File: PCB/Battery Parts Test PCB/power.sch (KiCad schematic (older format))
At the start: 28 parts, among them P4 CONN_2, P5 PWR_SWITCH, P6 CONN_2, Q10 FET_N, Q11 FET_N, Q9 FET_N, U1 ISL94203

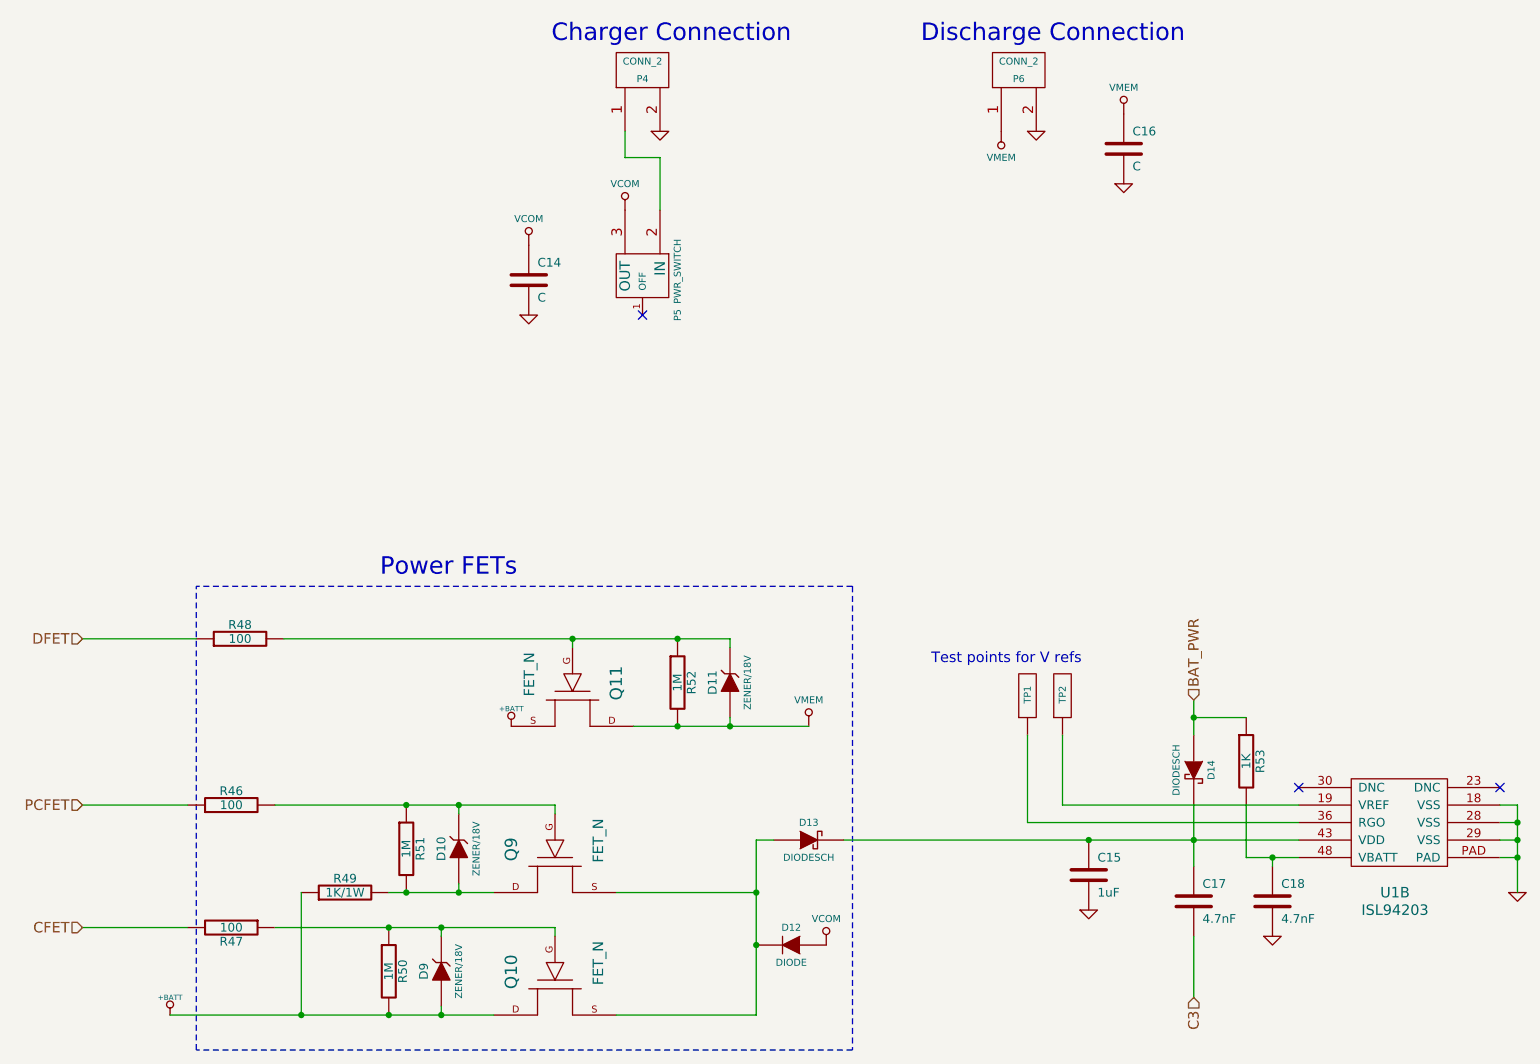
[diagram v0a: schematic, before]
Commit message: finished schematic with new battery monitor
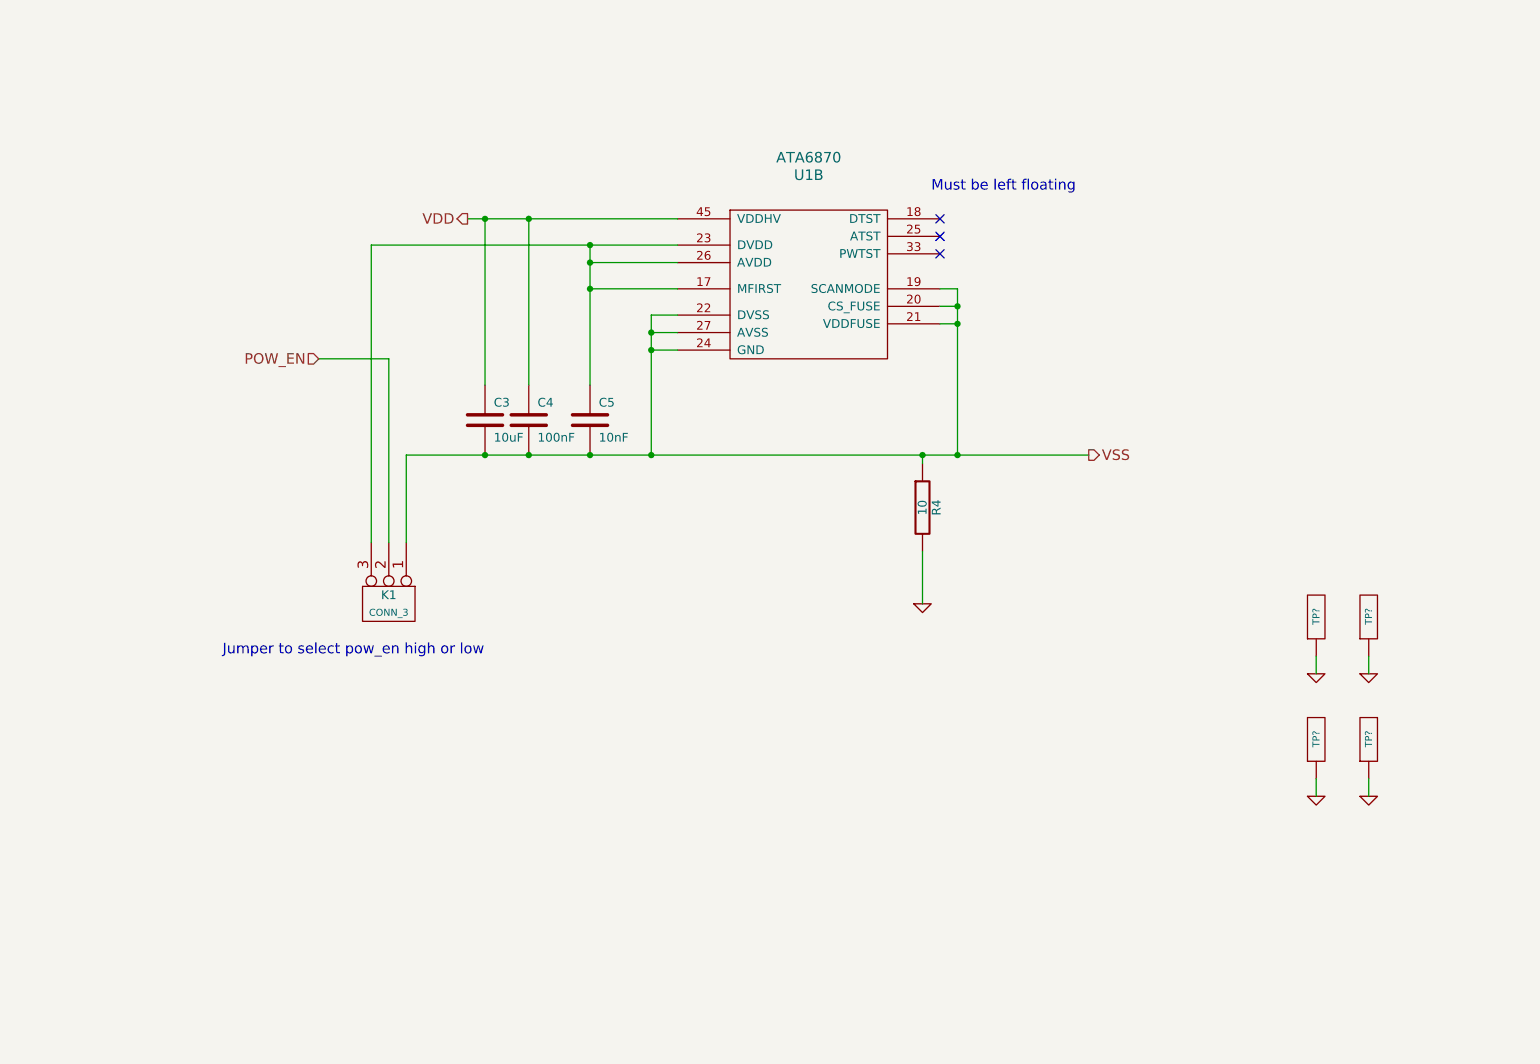
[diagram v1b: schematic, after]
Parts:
- removed C14, C16: C, symbol C
- removed C15: 1uF, symbol C
- removed C17, C18: 4.7nF, symbol C
- removed D10, D11, D9: ZENER/18V, symbol ZENER
- removed D12: DIODE, symbol DIODE
- removed D13, D14: DIODESCH, symbol DIODESCH
- removed P4, P6: CONN_2, symbol CONN_2
- removed P5: PWR_SWITCH, symbol PWR_SWITCH
- removed Q10, Q11, Q9: FET_N, symbol FET_N
- removed R46, R47, R48: 100, symbol R
- removed R49: 1K/1W, symbol R
- removed R50, R51, R52: 1M, symbol R
- removed R53: 1K, symbol R
- removed TP1, TP2: TEST_POINT, symbol TEST_POINT
- removed U1: ISL94203, symbol ISL94203
- added C3: 10uF, symbol C
- added C4: 100nF, symbol C
- added C5: 10nF, symbol C
- added K1: CONN_3, symbol CONN_3
- added R4: 10, symbol R
- added TP? (x4): TEST_POINT, symbol TEST_POINT
- added U1: ATA6870, symbol ATA6870
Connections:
- net GND: now also R4.2, TP?.1, TP?.1, TP?.1, TP?.1
- new net: C5.1, K1.3 (P3), U1.17 (MFIRST), U1.23 (DVDD), U1.26 (AVDD)
- new net POW_EN: K1.2 (PM)
- new net VDD: C3.1, C4.1, U1.45 (VDDHV)
- new net VSS: C3.2, C4.2, C5.2, K1.1 (P1), R4.1, U1.19 (SCANMODE), U1.20 (CS_FUSE), U1.21 (VDDFUSE), U1.22 (DVSS), U1.24 (GND), U1.27 (AVSS)
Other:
- note added: "Jumper to select pow_en high or low"
- note added: "Must be left floating"
- note removed: "Charger Connection"
- note removed: "Discharge Connection"
- note removed: "Power FETs"
- note removed: "Test points for V refs"

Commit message: updated schematic
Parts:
- gave numbers to parts that had none: 4
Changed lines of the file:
@@
-EESchema Schematic File Version 2  date 4/30/2013 1:48:29 PM
+EESchema Schematic File Version 2  date 5/7/2013 3:13:49 PM
 LIBS:power
 LIBS:device
@@
 Sheet 3 9
 Title ""
-Date "30 apr 2013"
+Date "7 may 2013"
 Rev ""
 Comp ""
@@
 $EndDescr
 $Comp
-L TEST_POINT TP?
+L TEST_POINT TP5
 U 1 1 5178A9A6
 P 8800 5200
-F 0 "TP?" H 8830 5200 40  0000 L CNN
+F 0 "TP5" H 8830 5200 40  0000 L CNN
 F 1 "TEST_POINT" H 8900 5105 30  0001 C CNN
 	1    8800 5200
@@
 $EndComp
 $Comp
-L GND #PWR?
+L GND #PWR01
 U 1 1 5178A9A5
 P 8800 5450
-F 0 "#PWR?" H 8800 5450 30  0001 C CNN
+F 0 "#PWR01" H 8800 5450 30  0001 C CNN
 F 1 "GND" H 8800 5380 30  0001 C CNN
 	1    8800 5450
@@
 	9100 5350 9100 5450
 $Comp
-L GND #PWR?
+L GND #PWR02
 U 1 1 5178A9A4
 P 9100 5450
-F 0 "#PWR?" H 9100 5450 30  0001 C CNN
+F 0 "#PWR02" H 9100 5450 30  0001 C CNN
 F 1 "GND" H 9100 5380 30  0001 C CNN
 	1    9100 5450
@@
 $EndComp
 $Comp
-L TEST_POINT TP?
+L TEST_POINT TP7
 U 1 1 5178A9A3
 P 9100 5200
-F 0 "TP?" H 9130 5200 40  0000 L CNN
+F 0 "TP7" H 9130 5200 40  0000 L CNN
 F 1 "TEST_POINT" H 9200 5105 30  0001 C CNN
 	1    9100 5200
@@
 $EndComp
 $Comp
-L TEST_POINT TP?
+L TEST_POINT TP6
 U 1 1 5178A9A2
 P 9100 4500
-F 0 "TP?" H 9130 4500 40  0000 L CNN
+F 0 "TP6" H 9130 4500 40  0000 L CNN
 F 1 "TEST_POINT" H 9200 4405 30  0001 C CNN
 	1    9100 4500
@@
 $EndComp
 $Comp
-L GND #PWR?
+L GND #PWR03
 U 1 1 5178A9A1
 P 9100 4750
-F 0 "#PWR?" H 9100 4750 30  0001 C CNN
+F 0 "#PWR03" H 9100 4750 30  0001 C CNN
 F 1 "GND" H 9100 4680 30  0001 C CNN
 	1    9100 4750
@@
 	8800 4650 8800 4750
 $Comp
-L GND #PWR?
+L GND #PWR04
 U 1 1 5178A9A0
 P 8800 4750
-F 0 "#PWR?" H 8800 4750 30  0001 C CNN
+F 0 "#PWR04" H 8800 4750 30  0001 C CNN
 F 1 "GND" H 8800 4680 30  0001 C CNN
 	1    8800 4750
@@
 $EndComp
 $Comp
-L TEST_POINT TP?
+L TEST_POINT TP4
 U 1 1 5178A99F
 P 8800 4500
-F 0 "TP?" H 8830 4500 40  0000 L CNN
+F 0 "TP4" H 8830 4500 40  0000 L CNN
 F 1 "TEST_POINT" H 8900 4405 30  0001 C CNN
 	1    8800 4500
@@
 $EndComp
 $Comp
-L GND #PWR1
+L GND #PWR05
 U 1 1 5178A293
 P 6550 4350
-F 0 "#PWR1" H 6550 4350 30  0001 C CNN
+F 0 "#PWR05" H 6550 4350 30  0001 C CNN
 F 1 "GND" H 6550 4280 30  0001 C CNN
 	1    6550 4350
